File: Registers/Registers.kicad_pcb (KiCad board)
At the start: 2 copper layers, 85 x 99.5 mm, 32 parts, among them J1 Output to Display, J2 Reg Specific Connections, J3 LED Wire Bus, J4 LED Wire Bus, U1 74HC173, U2 74HC173, U3 74HC245, U4 ATtiny84-20P

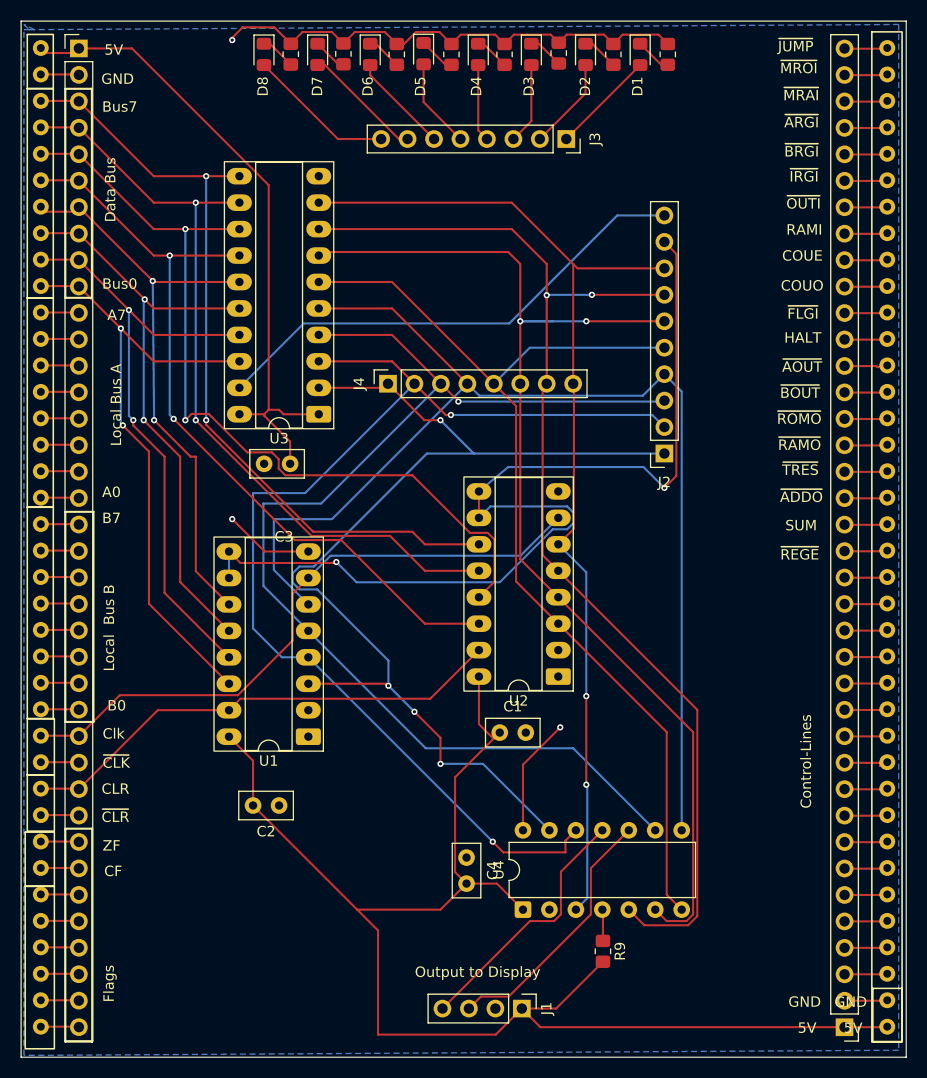
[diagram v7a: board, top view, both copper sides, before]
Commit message: Autorouted version of the board.
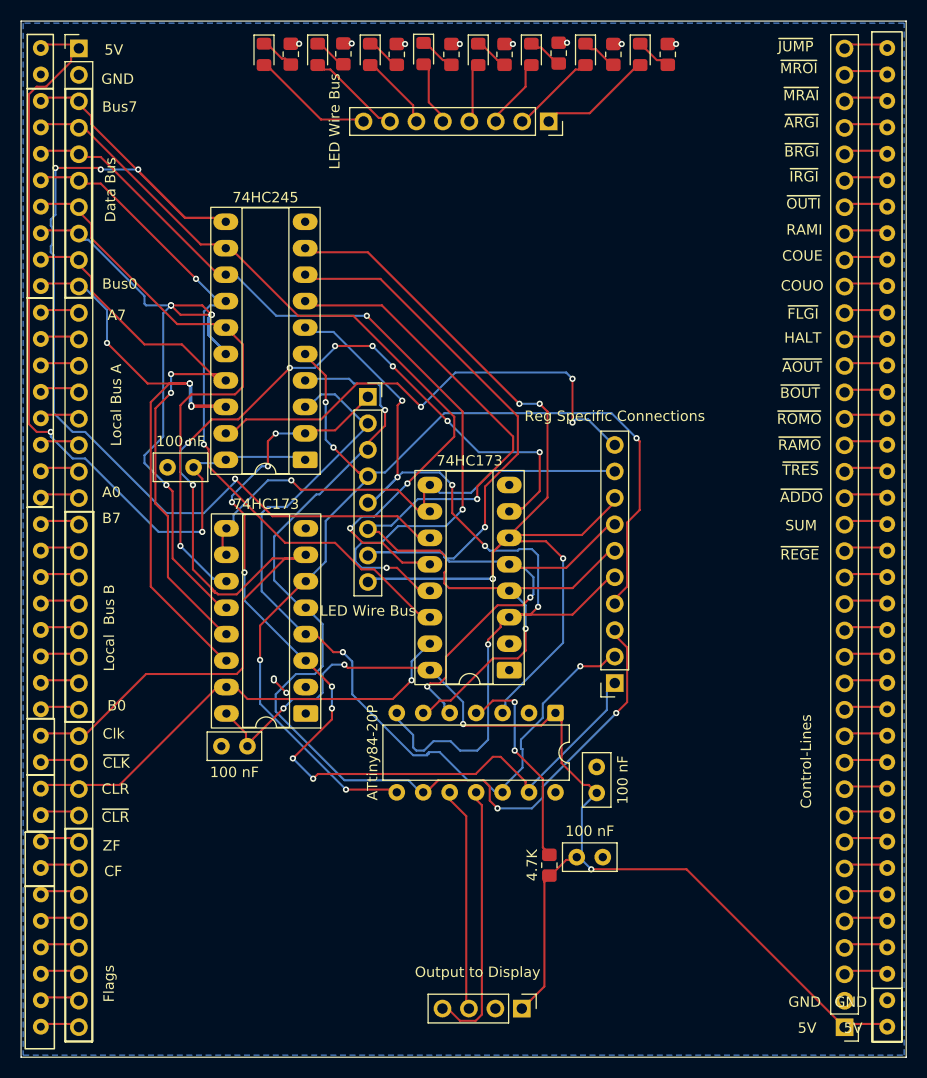
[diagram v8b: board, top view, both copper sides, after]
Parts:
- moved J2 22.5 mm to (80.7, 92.2)
- moved U4 19.1 mm to (75.0, 95.1), turned to -90 degrees
- moved C4 13.1 mm to (79.6, 109.0), turned to 180 degrees
- moved C1 11.0 mm to (79.0, 102.8), turned to 90 degrees
- moved R9 9.74 mm to (74.5, 109.7)
- moved C3 9.28 mm to (40.3, 71.5)
- moved C2 7.94 mm to (43.0, 98.3), turned to 0 degrees
- moved U2 4.75 mm to (70.6, 91.0)
- moved U3 4.57 mm to (51.0, 70.8)
- moved J3 2.39 mm to (74.4, 38.3)
- moved J4 2.31 mm to (57.0, 64.8), turned to 0 degrees
- moved U1 2.24 mm to (51.1, 95.2)
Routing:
- net GND: track 76.8 -> 21.1 mm, vias 3 -> 11
- net CLOCK: track 61.3 -> 112.2 mm, vias 0 -> 8
- net ~{RIN}: track 96.7 -> 47.5 mm, vias 2 -> 1
- net BUS7: track 77.1 -> 109.6 mm, vias 2 -> 4
- net REG1: track 110.1 -> 81.1 mm
- net 5V_2: track 136.2 -> 112.2 mm, vias 0 -> 4
- net REG5: track 110.6 -> 92.2 mm
- net Net-(U4-~{RESET}/PB3): track 3.02 -> 20.2 mm, vias 0 -> 2
- net 5V: track 64.0 -> 81.0 mm, vias 0 -> 2
- net REG0: track 103.8 -> 89.0 mm, vias 4 -> 8
- net REG2: track 113.0 -> 100.2 mm, vias 1 -> 3
- net REG3: track 115.5 -> 103.4 mm, vias 0 -> 5
- net REG6: track 111.6 -> 99.6 mm, vias 2 -> 3
- net REG7: track 100.1 -> 111.6 mm, vias 2 -> 5
- net BUS2: track 57.6 -> 67.1 mm, vias 2 -> 5
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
